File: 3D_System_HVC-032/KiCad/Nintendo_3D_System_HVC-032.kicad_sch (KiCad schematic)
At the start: 45 parts, among them CN1 Famicon Expansion Port, J1 スコープ１, J2 スコープ２, Q1 2SC2120, U1 Sharp IX0043AE, U2 JRC 4558D, X1 4MHz

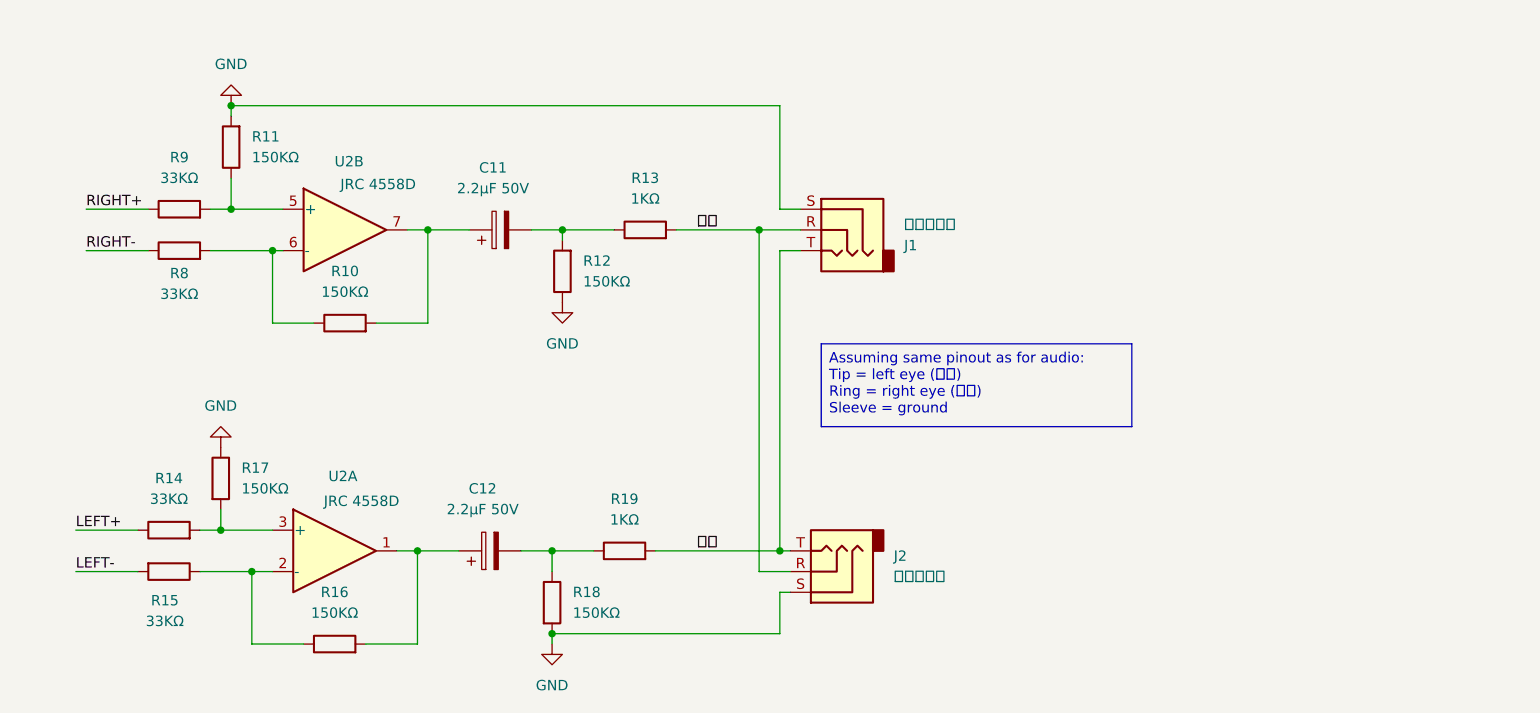
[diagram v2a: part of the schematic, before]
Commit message: Captured signalling
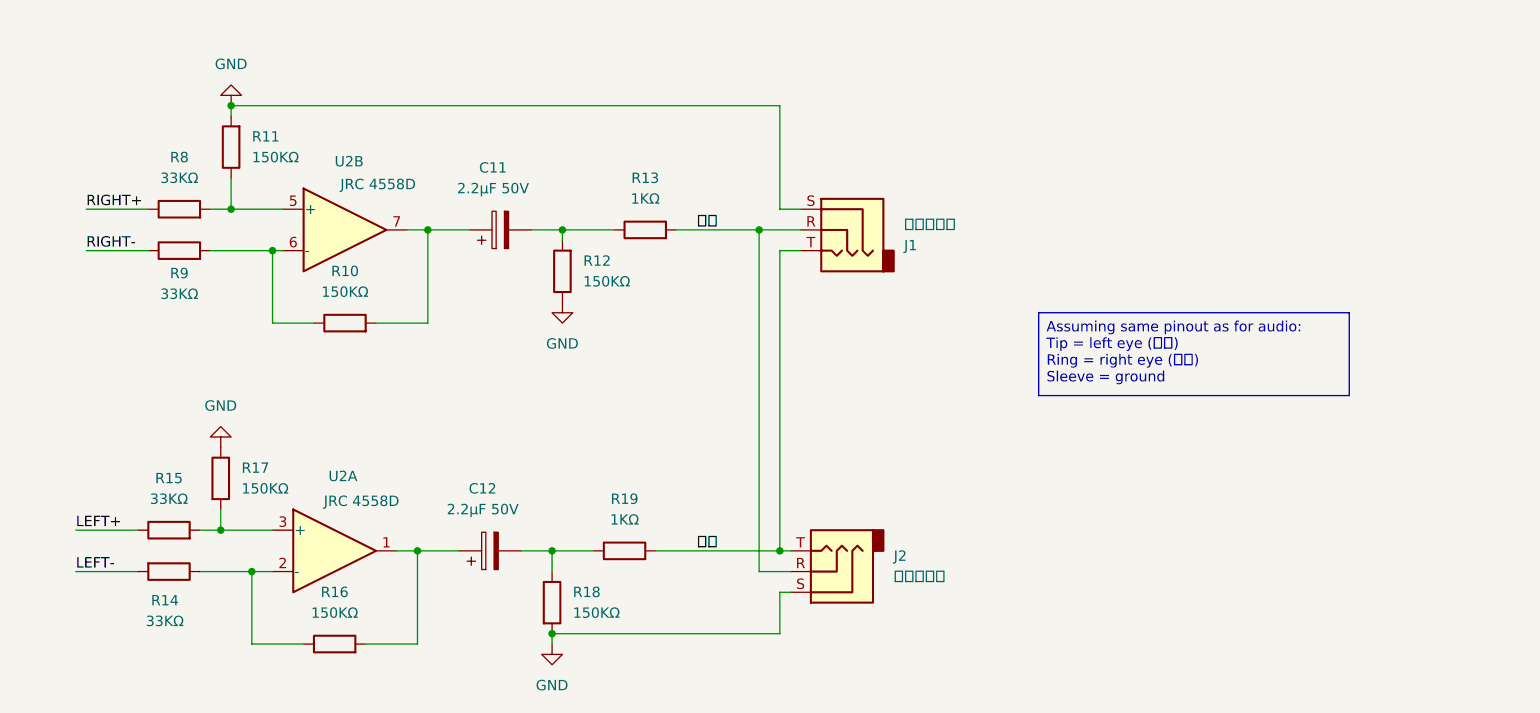
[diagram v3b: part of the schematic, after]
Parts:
- renumbered R15 to R14, R14 to R15, R9 to R8, R8 to R9
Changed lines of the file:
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@@
 	(text_box "Assuming same pinout as for audio:\nTip = left eye (左目)\nRing = right eye (右目)\nSleeve = ground"
 		(exclude_from_sim no)
-		(at 135.89 143.51 0)
+		(at 162.56 139.7 0)
 		(size 38.1 10.16)
 		(margins 0.9525 0.9525 0.9525 0.9525)
@@
 		(dnp no)
 		(fields_autoplaced yes)
-		(property "Reference" "R9"
+		(property "Reference" "R8"
 			(at 57.15 120.65 90)
 			(effects
@@
 			(project ""
 				(path "/2dee9d8b-2258-4eee-804b-ae751f82a888"
-					(reference "R9")
+					(reference "R8")
 					(unit 1)
 				)
@@
 		(on_board yes)
 		(dnp no)
-		(property "Reference" "R15"
+		(property "Reference" "R14"
 			(at 55.372 175.006 90)
 			(effects
@@
 			(project ""
 				(path "/2dee9d8b-2258-4eee-804b-ae751f82a888"
-					(reference "R15")
+					(reference "R14")
 					(unit 1)
 				)
@@
 		(dnp no)
 		(fields_autoplaced yes)
-		(property "Reference" "R14"
+		(property "Reference" "R15"
 			(at 55.88 160.02 90)
 			(effects
@@
 			(project ""
 				(path "/2dee9d8b-2258-4eee-804b-ae751f82a888"
-					(reference "R14")
+					(reference "R15")
 					(unit 1)
 				)
@@
 		(on_board yes)
 		(dnp no)
-		(property "Reference" "R8"
+		(property "Reference" "R9"
 			(at 57.15 134.874 90)
 			(effects
@@
 			(project ""
 				(path "/2dee9d8b-2258-4eee-804b-ae751f82a888"
-					(reference "R8")
+					(reference "R9")
 					(unit 1)
 				)
